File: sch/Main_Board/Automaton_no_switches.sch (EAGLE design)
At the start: 16 parts, among them IC1 74LS595D, IC2 74LS595D, IC3 74LS595D, IC4 74LS595D, J1 POWER_JACKPTH

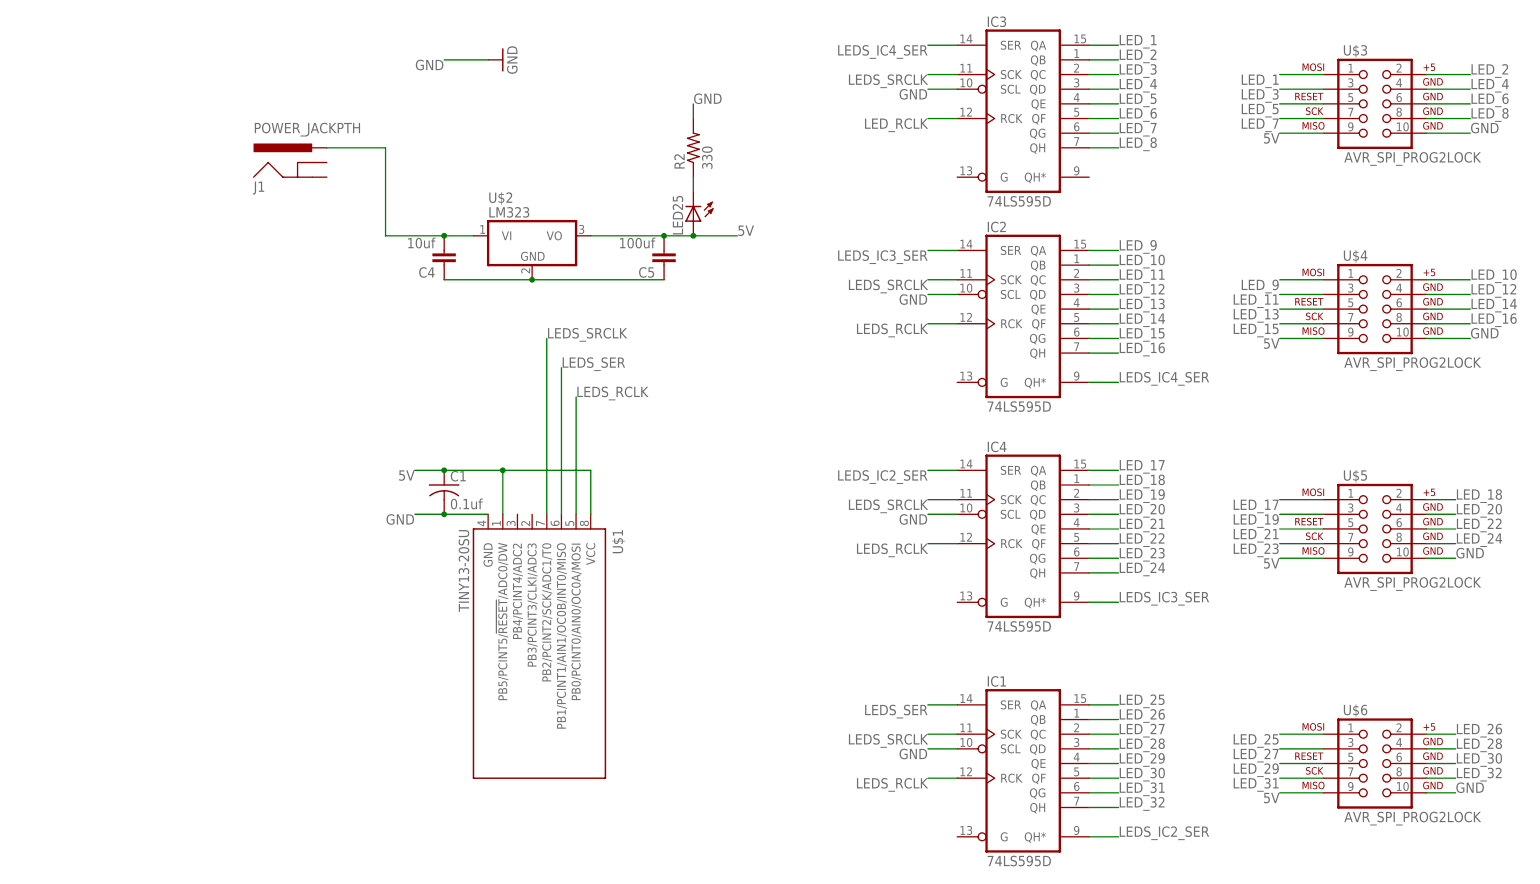
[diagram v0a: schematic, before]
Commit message: More schematic work.  Make a potentially working board for the main automaton circuit.
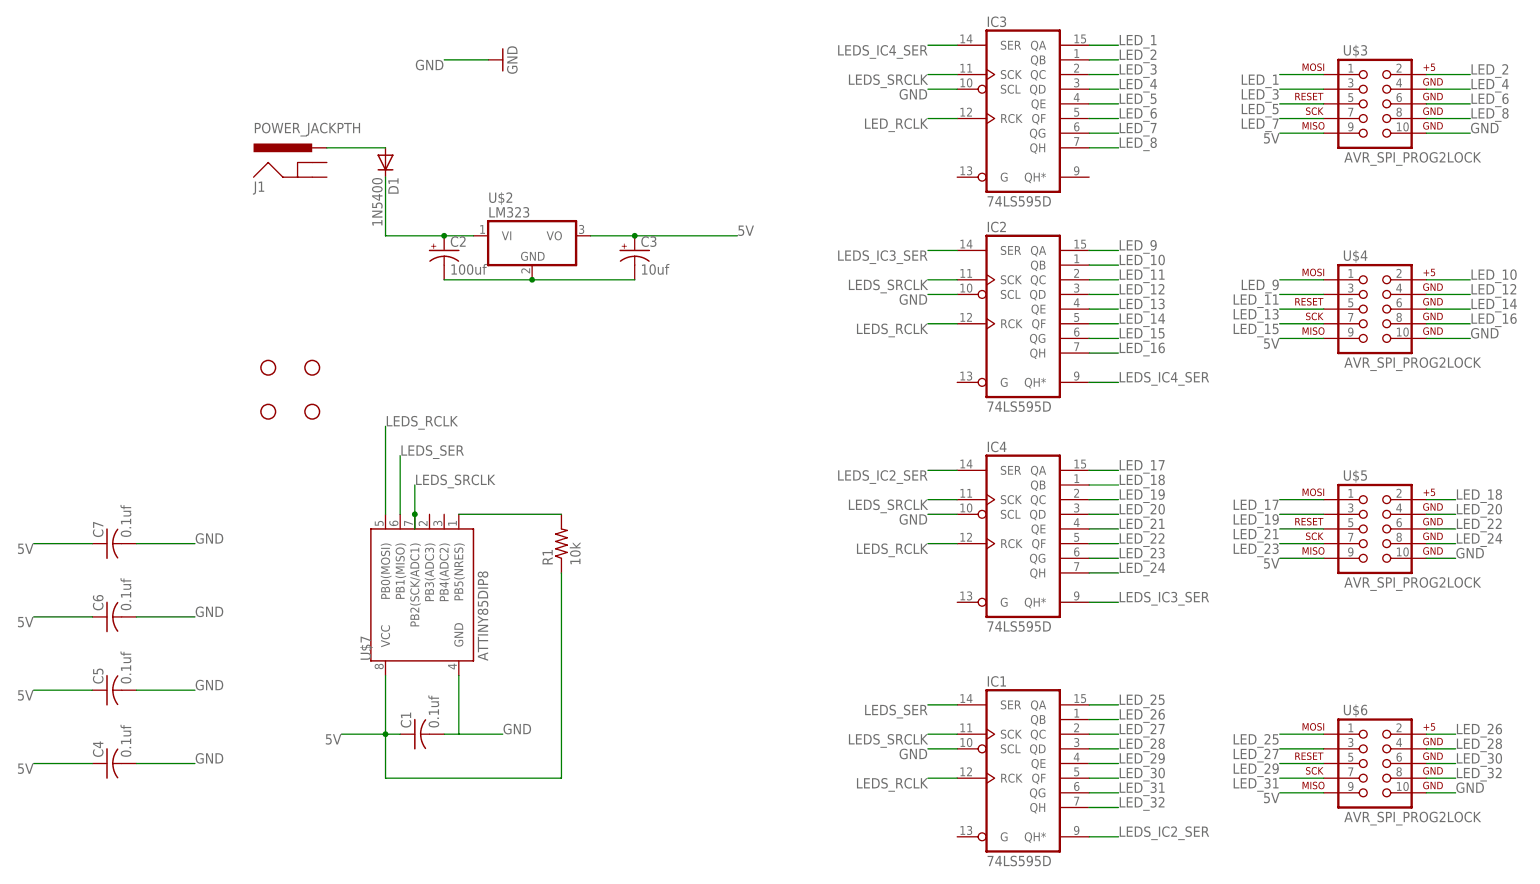
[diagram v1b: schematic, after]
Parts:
- removed LED25: (no value), led:LED
- removed R2: 330, resistor:R-US_0204/5
- removed U$1: TINY13-20SU, MyAtmel:TINY13-20SU
- added C2: 100uf, rcl:CPOL-USE5-10.5
- added C3: 10uf, rcl:CPOL-USE2-5
- added C6, C7: 0.1uf, resistor:C-US025-024X044
- added D1: 1N5400, diode:1N5400
- added JP1, JP2, JP3, JP4: STAND-OFF, SparkFun-Electromechanical:STAND-OFF
- added R1: 10k, resistor:R-US_M1206
- added U$7: ATTINY85DIP8, *Personal Library:ATTINY85DIP8
- C4: value 10uf -> 0.1uf; device SparkFun:CAP1210 -> resistor:C-US025-024X044
- C5: value 100uf -> 0.1uf; device SparkFun:CAP1210 -> resistor:C-US025-024X044
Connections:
- removed net N$27: LED25.C, R2.1
- new net N$2: R1.2, U$7.PB5(NRES)
- new net N$3: D1.A, J1.PWR
- net 5V: now also C3.+, C4.1, C5.1, C6.1, C7.1, R1.1, U$7.VCC; no longer C5.2, LED25.A, U$1.PB5/PCINT5/!RESET!/ADC0/DW, U$1.VCC
- net GND: now also C4.2, C5.2, C6.2, C7.2, U$7.GND; no longer R2.2, U$1.GND
- net LEDS_RCLK: now also U$7.PB0(MOSI); no longer U$1.PB0/PCINT0/AIN0/OC0A/MOSI
- net LEDS_SER: now also U$7.PB1(MISO); no longer U$1.PB1/PCINT1/AIN1/OC0B/INT0/MISO
- net LEDS_SRCLK: now also U$7.PB2(SCK/ADC1); no longer U$1.PB2/PCINT2/SCK/ADC1/T0
- net N$1: now also C2.+, D1.C; no longer C4.2, J1.PWR
- net N$4: now also C2.-, C3.-; no longer C4.1, C5.1
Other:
- moved on the sheet: C1, C4, C5
